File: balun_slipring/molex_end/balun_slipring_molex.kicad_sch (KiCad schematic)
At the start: 7 parts, among them J1 5055680471 / PINMAP TBD, J2 SMA_A, J3 SMA_B, T1 ADT2-1T+, T2 ADT2-1T+

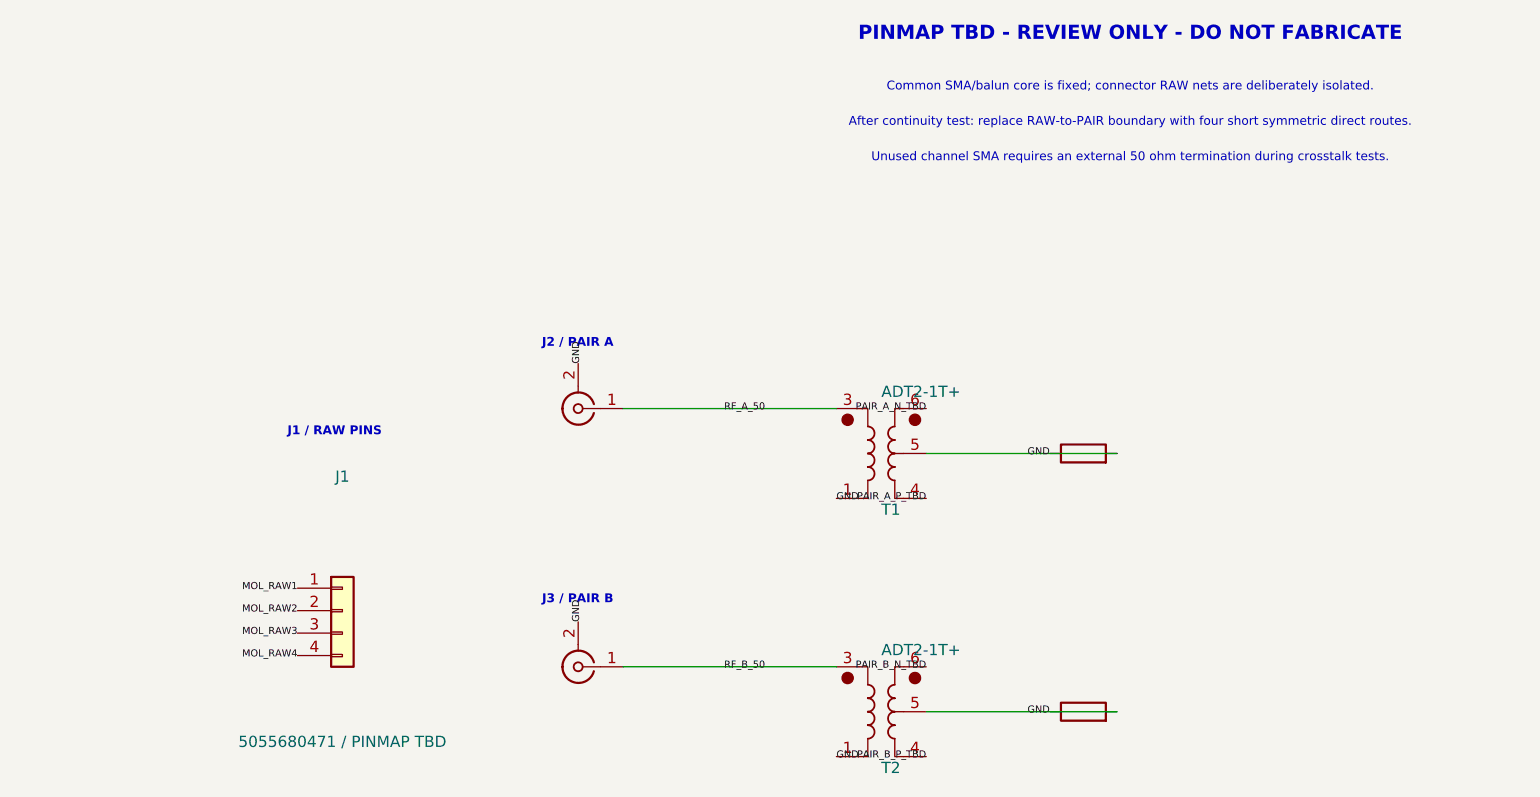
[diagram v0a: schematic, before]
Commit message: feat: finalize slip-ring fixtures and floating CT baseline
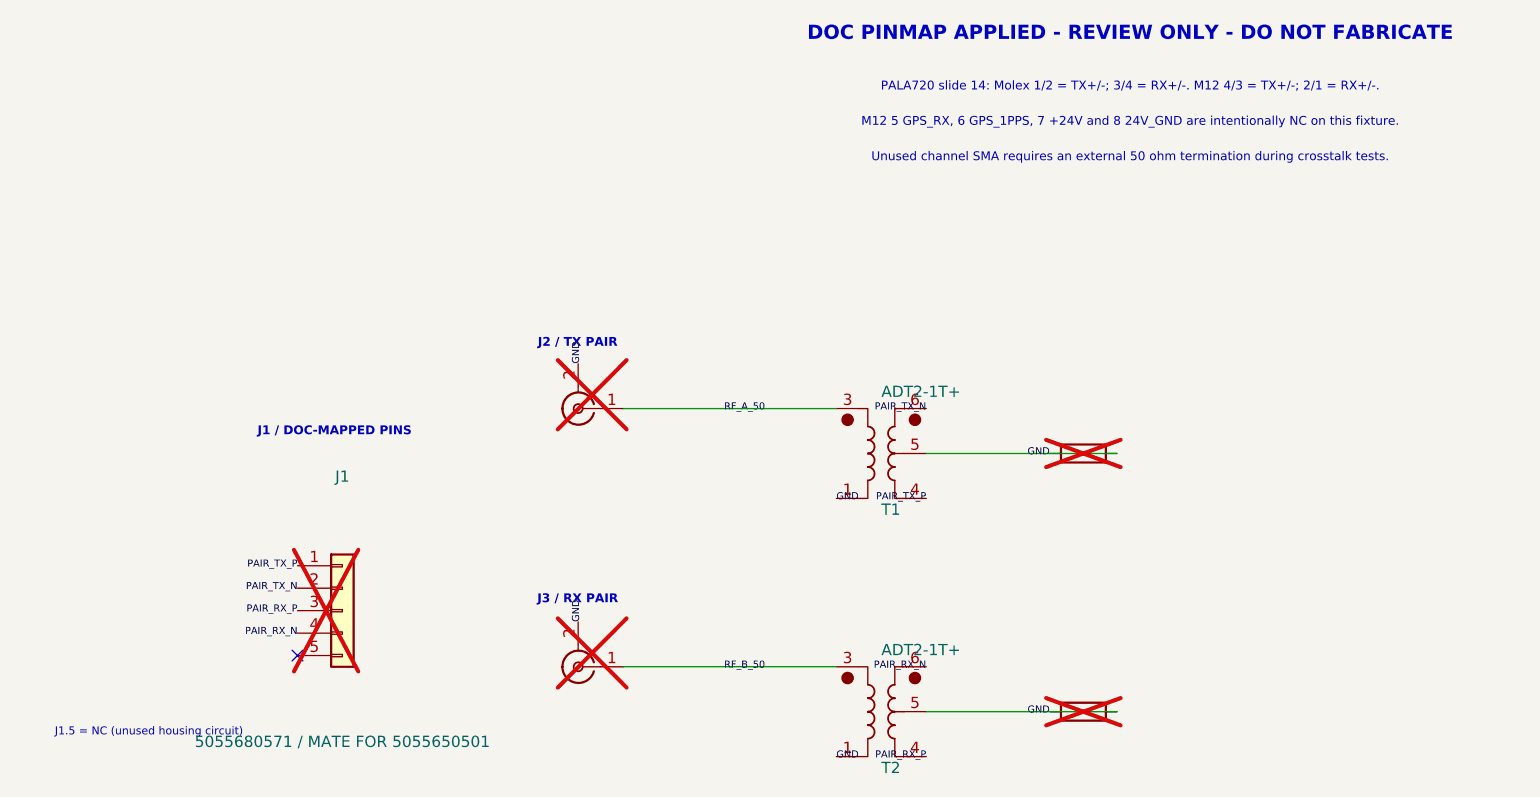
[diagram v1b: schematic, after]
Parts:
- J1: value 5055680471 / PINMAP TBD -> 5055680571 / MATE FOR 5055650501; footprint balun_slipring_common:Molex_5055680471 -> balun_slipring_common:Molex_5055680571; symbol Connector_Generic:Conn_01x04 -> Connector_Generic:Conn_01x05; Assembly FOOTPRINT PLACED; SIGNAL PINMAP TBD / DO NOT FABRICATE -> DNP UNTIL PHYSICAL MATING, KEY/PIN-1 ORIENTATION AND LAND P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; MPN 5055680471 -> 5055680571; now not fitted
- J2, J3: now not fitted
- RCT1, RCT2: Assembly FIT; remove for floating-CT comparison -> DNP; fit all four RCTs only for controlled CT-GND comparison; now not fitted
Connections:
- net PAIR_A_N_TBD is gone; now on net PAIR_TX_N: T1.6
- net PAIR_A_P_TBD is gone; now on net PAIR_TX_P: T1.4
- net PAIR_B_N_TBD is gone; now on net PAIR_RX_N: T2.6
- net PAIR_B_P_TBD is gone; now on net PAIR_RX_P: T2.4
- net MOL_RAW1 renamed PAIR_TX_P
- net MOL_RAW2 renamed PAIR_TX_N
- net MOL_RAW3 renamed PAIR_RX_P
- net MOL_RAW4 renamed PAIR_RX_N
- no-connect marks 0 -> 1
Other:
- note added: "DOC PINMAP APPLIED - REVIEW ONLY - DO NOT FABRICATE"
- note added: "J1 / DOC-MAPPED PINS"
- note added: "J1.5 = NC (unused housing circuit)"
- note added: "J2 / TX PAIR"
- note added: "J3 / RX PAIR"
- note added: "M12 5 GPS_RX, 6 GPS_1PPS, 7 +24V and 8 24V_GND are intentionally NC on this fixture."
- note added: "PALA720 slide 14: Molex 1/2 = TX+/-; 3/4 = RX+/-. M12 4/3 = TX+/-; 2/1 = RX+/-."
- note removed: "After continuity test: replace RAW-to-PAIR boundary with four short symmetric direct routes."
- note removed: "Common SMA/balun core is fixed; connector RAW nets are deliberately isolated."
- note removed: "J1 / RAW PINS"
- note removed: "J2 / PAIR A"
- note removed: "J3 / PAIR B"
- note removed: "PINMAP TBD - REVIEW ONLY - DO NOT FABRICATE"
- title: 100BASE-TX slip-ring VNA fixture - MOLEX END - PINMAP TBD -> 100BASE-TX slip-ring VNA fixture - MOLEX END - DOC PINMAP
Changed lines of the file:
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@@
 	(paper "A4")
 	(title_block
-		(title "100BASE-TX slip-ring VNA fixture - MOLEX END - PINMAP TBD")
+		(title "100BASE-TX slip-ring VNA fixture - MOLEX END - DOC PINMAP")
 		(date "2026-08-13")
-		(rev "DRAFT 0")
+		(rev "DRAFT 1")
 		(comment 1 "Two-channel 50 ohm single-ended to 100 ohm differential fixture core.")
-		(comment 2 "Connector RAW pins intentionally not mapped to balun pairs.")
-		(comment 3 "REVIEW ONLY - DO NOT FABRICATE UNTIL PINMAP AND CONNECTOR MECHANICS ARE VERIFIED.")
-	)
-	(text "PINMAP TBD - REVIEW ONLY - DO NOT FABRICATE"
+		(comment 2 "Electrical map from PALA720 slide 14; TX and RX fan-outs are connected.")
+		(comment 3 "REVIEW ONLY - DO NOT FABRICATE UNTIL CONTINUITY, CONNECTOR MECHANICS AND SMA STACK ARE VERIFIED.")
+	)
+	(text "DOC PINMAP APPLIED - REVIEW ONLY - DO NOT FABRICATE"
 		(exclude_from_sim no)
 		(at 145 25 0)
@@
 		)
 	)
-	(text "Common SMA/balun core is fixed; connector RAW nets are deliberately isolated."
+	(text "PALA720 slide 14: Molex 1/2 = TX+/-; 3/4 = RX+/-. M12 4/3 = TX+/-; 2/1 = RX+/-."
 		(exclude_from_sim no)
 		(at 145 31 0)
@@
 		)
 	)
-	(text "After continuity test: replace RAW-to-PAIR boundary with four short symmetric direct routes."
+	(text "M12 5 GPS_RX, 6 GPS_1PPS, 7 +24V and 8 24V_GND are intentionally NC on this fixture."
 		(exclude_from_sim no)
 		(at 145 35 0)
@@
 		)
 	)
-	(text "J2 / PAIR A"
+	(text "J2 / TX PAIR"
 		(exclude_from_sim no)
 		(at 82.5 60 0)
@@
 		)
 	)
-	(text "J3 / PAIR B"
+	(text "J3 / RX PAIR"
 		(exclude_from_sim no)
 		(at 82.5 89 0)
@@
 		)
 	)
-	(text "J1 / RAW PINS"
+	(text "J1 / DOC-MAPPED PINS"
 		(exclude_from_sim no)
 		(at 55 70 0)
@@
 		)
 	)
-	(label "PAIR_A_N_TBD"
+	(label "PAIR_TX_N"
 		(at 121.92 67.31 180)
 		(effects
@@
 		)
 	)
-	(label "PAIR_A_P_TBD"
+	(label "PAIR_TX_P"
 		(at 121.92 77.47 180)
 		(effects
@@
 		)
 	)
-	(label "PAIR_B_N_TBD"
+	(label "PAIR_RX_N"
 		(at 121.92 96.52 180)
 		(effects
@@
 		)
 	)
-	(label "PAIR_B_P_TBD"
+	(label "PAIR_RX_P"
 		(at 121.92 106.68 180)
 		(effects
@@
 		)
 	)
-	(label "MOL_RAW1"
+	(label "PAIR_TX_P"
+		(at 50.8 85.09 180)
+		(effects
+			(font
+				(size 0.8 0.8)
+			)
+		)
+	)
+	(label "PAIR_TX_N"
 		(at 50.8 87.63 180)
 		(effects
@@
 		)
 	)
-	(label "MOL_RAW2"
+	(label "PAIR_RX_P"
 		(at 50.8 90.17 180)
 		(effects
@@
 		)
 	)
-	(label "MOL_RAW3"
+	(label "PAIR_RX_N"
 		(at 50.8 92.71 180)
 		(effects
@@
 		)
 	)
-	(label "MOL_RAW4"
-		(at 50.8 95.25 180)
-		(effects
-			(font
-				(size 0.8 0.8)
+	(no_connect
+		(at 50.8 95.25)
+	)
+	(text "J1.5 = NC (unused housing circuit)"
+		(exclude_from_sim no)
+		(at 34 104 0)
+		(effects
+			(font
+				(size 0.9 0.9)
 			)
 		)
@@
 			(in_bom yes)
 			(on_board yes)
-			(in_pos_files yes)
-			(dnp no)
+			(in_pos_files no)
+			(dnp yes)
 			(property "Reference" "J2"
 				(at 82.55 67.31 0)
@@
 			(in_bom yes)
 			(on_board yes)
-			(in_pos_files yes)
-			(dnp no)
+			(in_pos_files no)
+			(dnp yes)
 			(property "Reference" "J3"
 				(at 82.55 96.52 0)
@@
 			(in_bom yes)
 			(on_board yes)
-			(in_pos_files yes)
-			(dnp no)
+			(in_pos_files no)
+			(dnp yes)
 			(property "Reference" "RCT1"
 				(at 139.7 72.39 0)
@@
 				)
 			)
-			(property "Assembly" "FIT; remove for floating-CT comparison"
+			(property "Assembly" "DNP; fit all four RCTs only for controlled CT-GND comparison"
 				(at 142.24 77.4699 0)
 				(hide yes)
@@
 			(in_bom yes)
 			(on_board yes)
-			(in_pos_files yes)
-			(dnp no)
+			(in_pos_files no)
+			(dnp yes)
 			(property "Reference" "RCT2"
 				(at 139.7 101.6 0)
@@
 				)
 			)
-			(property "Assembly" "FIT; remove for floating-CT comparison"
+			(property "Assembly" "DNP; fit all four RCTs only for controlled CT-GND comparison"
 				(at 142.24 106.6799 0)
 				(hide yes)
@@
 		)
 	(symbol
-		(lib_id "Connector_Generic:Conn_01x04")
+		(lib_id "Connector_Generic:Conn_01x05")
 		(at 55.88 90.17 0)
 		(unit 1)
@@
 		(in_bom yes)
 		(on_board yes)
-		(in_pos_files yes)
-		(dnp no)
+		(in_pos_files no)
+		(dnp yes)
 		(property "Reference" "J1"
 			(at 55.88 75 0)
@@
 			)
 		)
-		(property "Value" "5055680471 / PINMAP TBD"
+		(property "Value" "5055680571 / MATE FOR 5055650501"
 			(at 55.88 105 0)
 			(show_name no)
@@
 			)
 		)
-		(property "Footprint" "balun_slipring_common:Molex_5055680471"
+		(property "Footprint" "balun_slipring_common:Molex_5055680571"
 			(at 55.88 90.17 0)
 			(hide yes)
@@
 			)
 		)
-		(property "Datasheet" "https://www.molex.com/content/dam/molex/molex-dot-com/products/automated/en-us/2ddrawingdxfadobe2d/505/505568/5055680471.pdf?inline="
+		(property "Datasheet" "https://www.molex.com/en-us/products/part-detail/5055680571"
 			(at 55.88 90.17 0)
 			(hide yes)
@@
 			)
 		)
-		(property "Description" "Connector-side raw pins; intentionally isolated from balun pairs until continuity mapping is verified"
+		(property "Description" "Document-mapped five-circuit PCB-side candidate for the 5055650501 cable housing; circuit 5 is intentionally NC"
 			(at 55.88 90.17 0)
 			(hide yes)
@@
 			)
 		)
-		(property "MPN" "5055680471"
+		(property "MPN" "5055680571"
 			(at 55.88 90.17 0)
 			(hide yes)
@@
 			)
 		)
-		(property "Assembly" "FOOTPRINT PLACED; SIGNAL PINMAP TBD / DO NOT FABRICATE"
+		(property "Assembly" "DNP UNTIL PHYSICAL MATING, KEY/PIN-1 ORIENTATION AND LAND PATTERN ARE VERIFIED AGAINST REV-504"
 			(at 55.88 90.17 0)
 			(hide yes)
@@
 		(pin "4"
 		)
+		(pin "5"
+		)
 		(instances

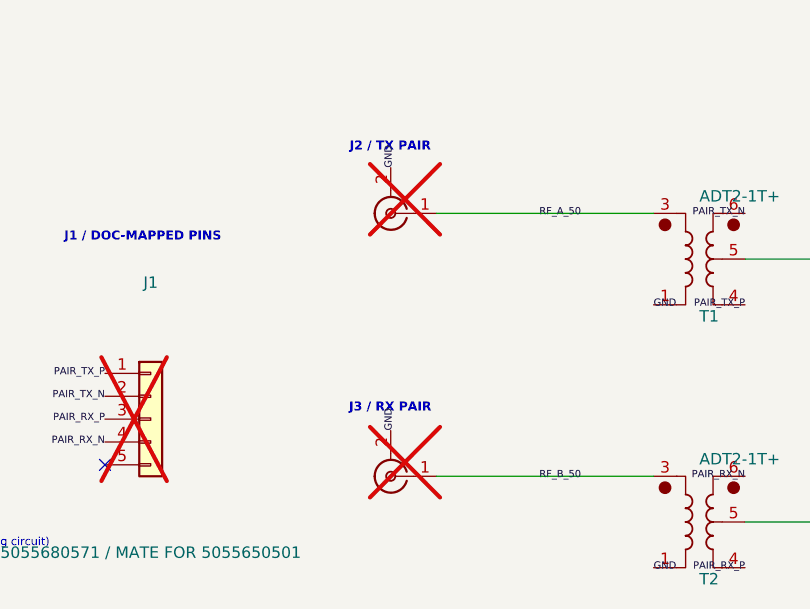
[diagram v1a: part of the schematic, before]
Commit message: feat: finalize JLC parts and measurement BOM
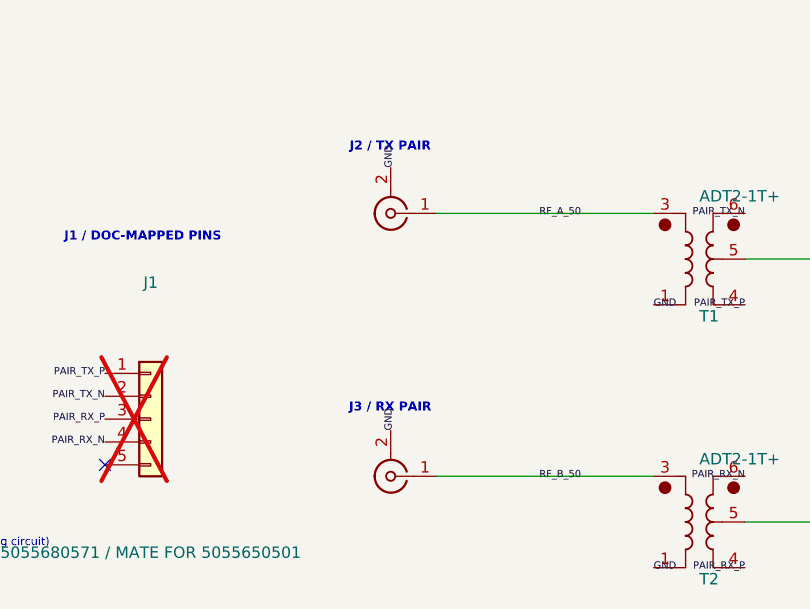
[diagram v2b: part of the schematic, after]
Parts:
- J1: LCSC Part # (none) -> C585386
- J2, J3: footprint Connector_Coaxial:SMA_Amphenol_132289_EdgeMount -> balun_slipring_common:SMA_MyAntenna_A-SMA-KE-16.5A_EdgeMount; Assembly DNP UNTIL STACK/CONNECTOR DECISION -> FIT; JLC C22467617; Standard PCBA / wave-solder review; LCSC Part # (none) -> C22467617; MPN 132289 -> A-SMA-KE-16.5A; Manufacturer Amphenol RF -> MyAntenna; now fitted
- RCT1, RCT2: LCSC Part # (none) -> C17477
- T1, T2: LCSC Part # (none) -> C5223988
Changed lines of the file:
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@@
 		(comment 1 "Two-channel 50 ohm single-ended to 100 ohm differential fixture core.")
 		(comment 2 "Electrical map from PALA720 slide 14; TX and RX fan-outs are connected.")
-		(comment 3 "REVIEW ONLY - DO NOT FABRICATE UNTIL CONTINUITY, CONNECTOR MECHANICS AND SMA STACK ARE VERIFIED.")
+		(comment 3 "REVIEW ONLY - DO NOT FABRICATE UNTIL CONTINUITY AND ENDPOINT CONNECTOR MECHANICS ARE VERIFIED.")
 	)
 	(text "DOC PINMAP APPLIED - REVIEW ONLY - DO NOT FABRICATE"
@@
 			(in_bom yes)
 			(on_board yes)
-			(in_pos_files no)
-			(dnp yes)
+			(in_pos_files yes)
+			(dnp no)
 			(property "Reference" "J2"
 				(at 82.55 67.31 0)
@@
 				)
 			)
-			(property "Footprint" "Connector_Coaxial:SMA_Amphenol_132289_EdgeMount"
+			(property "Footprint" "balun_slipring_common:SMA_MyAntenna_A-SMA-KE-16.5A_EdgeMount"
 				(at 82.55 67.31 0)
 				(hide yes)
@@
 				)
 			)
-			(property "Datasheet" "https://www.amphenolrf.com/132289.html"
+			(property "Datasheet" "https://datasheet.lcsc.com/datasheet/pdf/92633ab2cf30de4413e1a152c04a3ed5.pdf?productCode=C22467617"
 				(at 82.55 67.31 0)
 				(hide yes)
@@
 				)
 			)
-			(property "Manufacturer" "Amphenol RF"
+			(property "Manufacturer" "MyAntenna"
 				(at 85.09 72.3899 0)
 				(hide yes)
@@
 				)
 			)
-			(property "MPN" "132289"
+			(property "MPN" "A-SMA-KE-16.5A"
 				(at 85.09 72.3899 0)
 				(hide yes)
@@
 				)
 			)
-			(property "Assembly" "DNP UNTIL STACK/CONNECTOR DECISION"
+			(property "Assembly" "FIT; JLC C22467617; Standard PCBA / wave-solder review"
 				(at 85.09 72.3899 0)
 				(hide yes)
@@
 					)
 				)
+			)
+			(property "LCSC Part #" "C22467617"
+				(at 0 0 0)
+				(hide yes)
+				(show_name no)
+				(do_not_autoplace no)
+				(effects (font (size 1.27 1.27)))
 			)
 			(pin "1"
@@
 			(in_bom yes)
 			(on_board yes)
-			(in_pos_files no)
-			(dnp yes)
+			(in_pos_files yes)
+			(dnp no)
 			(property "Reference" "J3"
 				(at 82.55 96.52 0)
@@
 				)
 			)
-			(property "Footprint" "Connector_Coaxial:SMA_Amphenol_132289_EdgeMount"
+			(property "Footprint" "balun_slipring_common:SMA_MyAntenna_A-SMA-KE-16.5A_EdgeMount"
 				(at 82.55 96.52 0)
 				(hide yes)
@@
 				)
 			)
-			(property "Datasheet" "https://www.amphenolrf.com/132289.html"
+			(property "Datasheet" "https://datasheet.lcsc.com/datasheet/pdf/92633ab2cf30de4413e1a152c04a3ed5.pdf?productCode=C22467617"
 				(at 82.55 96.52 0)
 				(hide yes)
@@
 				)
 			)
-			(property "Manufacturer" "Amphenol RF"
+			(property "Manufacturer" "MyAntenna"
 				(at 85.09 101.5999 0)
 				(hide yes)
@@
 				)
 			)
-			(property "MPN" "132289"
+			(property "MPN" "A-SMA-KE-16.5A"
 				(at 85.09 101.5999 0)
 				(hide yes)
@@
 				)
 			)
-			(property "Assembly" "DNP UNTIL STACK/CONNECTOR DECISION"
+			(property "Assembly" "FIT; JLC C22467617; Standard PCBA / wave-solder review"
 				(at 85.09 101.5999 0)
 				(hide yes)
@@
 					)
 				)
+			)
+			(property "LCSC Part #" "C22467617"
+				(at 0 0 0)
+				(hide yes)
+				(show_name no)
+				(do_not_autoplace no)
+				(effects (font (size 1.27 1.27)))
 			)
 			(pin "1"
@@
 				)
 			)
+			(property "LCSC Part #" "C5223988"
+				(at 119.38 77.4699 0)
+				(hide yes)
+				(show_name no)
+				(do_not_autoplace no)
+				(effects
+					(font
+						(size 1.27 1.27)
+					)
+				)
+			)
 			(pin "1"
 			)
@@
 				)
 			)
+			(property "LCSC Part #" "C5223988"
+				(at 119.38 106.6799 0)
+				(hide yes)
+				(show_name no)
+				(do_not_autoplace no)
+				(effects
+					(font
+						(size 1.27 1.27)
+					)
+				)
+			)
 			(pin "1"
 			)
@@
 				)
 			)
+			(property "LCSC Part #" "C17477"
+				(at 142.24 77.4699 0)
+				(hide yes)
+				(show_name no)
+				(do_not_autoplace no)
+				(effects
+					(font
+						(size 1.27 1.27)
+					)
+				)
+			)
 			(pin "1"
 			)
@@
 			)
 			(property "Assembly" "DNP; fit all four RCTs only for controlled CT-GND comparison"
+				(at 142.24 106.6799 0)
+				(hide yes)
+				(show_name no)
+				(do_not_autoplace no)
+				(effects
+					(font
+						(size 1.27 1.27)
+					)
+				)
+			)
+			(property "LCSC Part #" "C17477"
 				(at 142.24 106.6799 0)
 				(hide yes)
@@
 			(at 55.88 90.17 0)
 			(hide yes)
+			(show_name no)
+			(do_not_autoplace no)
+			(effects
+				(font
+					(size 1.27 1.27)
+				)
+			)
+		)
+		(property "LCSC Part #" "C585386"
+			(at 55.88 90.17 0)
+			(hide yes)

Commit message: feat: add complete VNA fixture design set
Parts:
- J1: value 5055680571 / MATE FOR 5055650501 -> 5055680571 / 505565 SERIES MATE CAND
- RCT1, RCT2: MPN 0 ohm 0805 -> 0805W8F0000T5E; Manufacturer ANY -> UNI-ROYAL
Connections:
- net GND: no longer RCT1.2, RCT2.2, T1.5, T2.5
- new net: RCT1.2, T1.5
- new net: RCT2.2, T2.5
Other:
- note added: "1"
- note added: "1. REVIEW ONLY - DO NOT FABRICATE. Connector fit / mechanics remain on HOLD."
- note added: "1:2 impedance"
- note added: "2"
- note added: "2. Existing J1 DNP is retained as a candidate HOLD; not a connectorless order."
- note added: "3"
- note added: "3. RCT1/RCT2 DNP: CT-FLOAT baseline. No on-board 100 ohm load."
- note added: "4"
- note added: "4. M12 pins 5/6/7/8 are NC; disconnect power and all active equipment."
- note added: "5. Two-board tests: terminate the two unused SMA ports with 50 ohm loads."
- note added: "505565 cable mate candidate / HOLD"
- note added: "6. Coax O/S/L + THRU does not remove the balun / PCB / connector response."
- note added: "A / TX PAIR - 50 ohm SMA to 100 ohm differential"
- note added: "ASSEMBLY / MEASUREMENT NOTES"
- note added: "B / RX PAIR - 50 ohm SMA to 100 ohm differential"
- note added: "DNP / CT FLOAT"
- note added: "Logical pin numbers; verify mating-face / PCB view."
- note added: "M12"
- note added: "MOLEX"
- note added: "MOLEX END / J1"
- note added: "NOT interchangeable with the LLC / actuator M12 fixture."
- note added: "RX+"
- note added: "RX-"
- note added: "SIGNAL"
- note added: "SLIPRING / MOLEX END"
- note added: "SLIPRING MAP / PALA720 SLIDE 14"
- note added: "TX+"
- note added: "TX-"
- note added: "UNUSED / NC"
- note added: "슬립링 측정 지그 | MOLEX END"
- note removed: "DOC PINMAP APPLIED - REVIEW ONLY - DO NOT FABRICATE"
- note removed: "J1 / DOC-MAPPED PINS"
- note removed: "J1.5 = NC (unused housing circuit)"
- note removed: "J2 / TX PAIR"
- note removed: "J3 / RX PAIR"
- note removed: "M12 5 GPS_RX, 6 GPS_1PPS, 7 +24V and 8 24V_GND are intentionally NC on this fixture."
- note removed: "PALA720 slide 14: Molex 1/2 = TX+/-; 3/4 = RX+/-. M12 4/3 = TX+/-; 2/1 = RX+/-."
- note removed: "Unused channel SMA requires an external 50 ohm termination during crosstalk tests."
- title: 100BASE-TX slip-ring VNA fixture - MOLEX END - DOC PINMAP -> SLIPRING / MOLEX END
- moved on the sheet: J1, T1, T2
